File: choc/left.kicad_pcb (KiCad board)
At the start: 2 copper layers, 118 x 92 mm, 87 parts, among them J1 USB_B_Micro, SW1 SW_Push, SW10 SW_Push, SW11 SW_Push, SW12 SW_Push, SW13 SW_Push, SW14 SW_Push, SW15 SW_Push, SW16 SW_Push, SW17 SW_Push, SW18 SW_Push, SW19 SW_Push, SW2 SW_Push, SW20 SW_Push, SW21 SW_Push, SW22 SW_Push, SW23 SW_Push, SW3 SW_Push, SW4 SW_Push, SW47 SW_Push, SW49 SW_Push, SW5 SW_Push, SW6 SW_Push, SW7 SW_Push, SW8 SW_Push, SW9 SW_Push, U1 ProMicro

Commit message: progress
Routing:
- net GND: track 0.00 -> 753.6 mm, vias 0 -> 5
- net +5V: track 0.00 -> 578.4 mm, vias 0 -> 7
- net /lcol0: track 0.00 -> 183.0 mm, vias 0 -> 2
- net /lcol2: track 0.00 -> 176.5 mm, vias 0 -> 3
- net /lcol3: track 0.00 -> 174.6 mm, vias 0 -> 3
- net /lcol1: track 0.00 -> 156.9 mm, vias 0 -> 4
- net /lcol4: track 0.00 -> 111.5 mm, vias 0 -> 1
- net Net-(LED1-Pad4): track 0.00 -> 106.6 mm, vias 0 -> 2
- net /lrow4: track 0.00 -> 105.1 mm
- net /lrow0: track 0.00 -> 97.8 mm
- net Net-(LED23-Pad2): track 0.00 -> 96.3 mm
- net Net-(D2-Pad2): track 0.00 -> 96.1 mm
- net Net-(D3-Pad2): track 0.00 -> 87.8 mm, vias 0 -> 1
- net Net-(LED2-Pad4): track 0.00 -> 87.7 mm, vias 0 -> 2
- net /lrow1: track 0.00 -> 83.8 mm, vias 0 -> 2
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
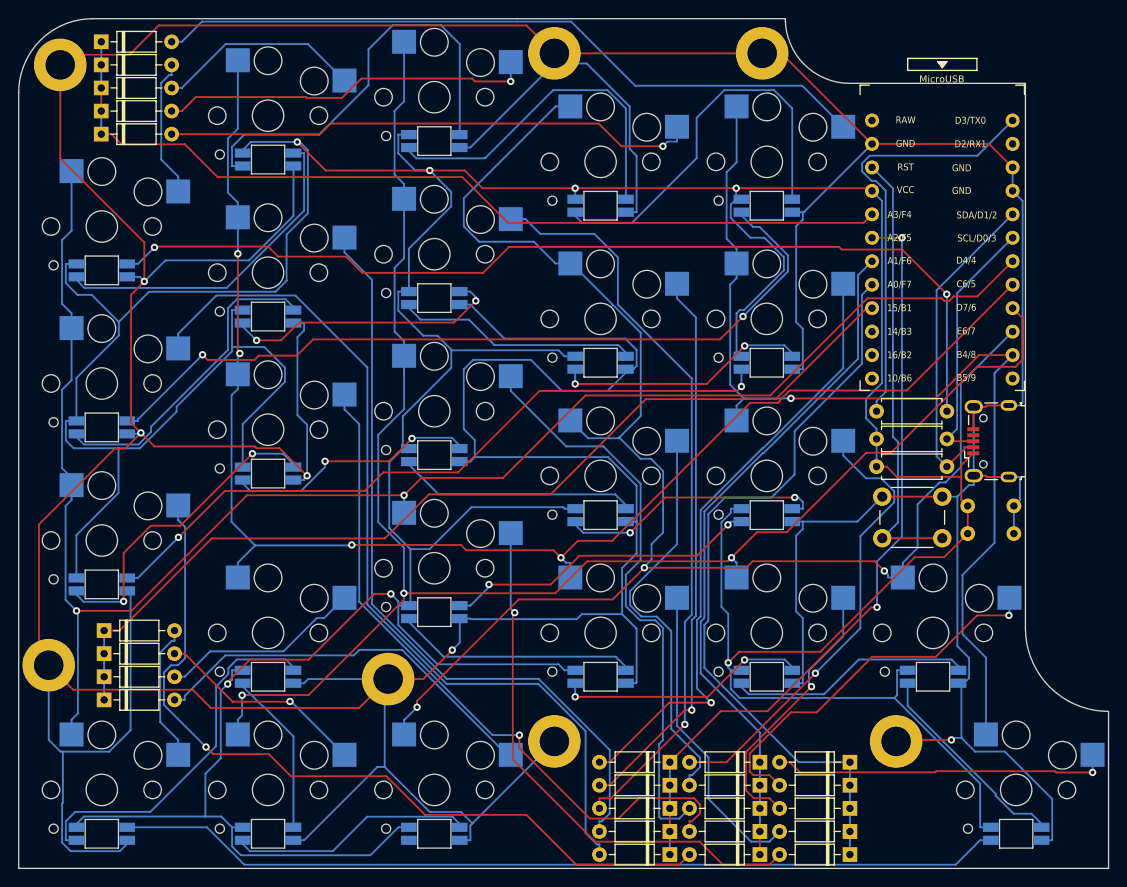
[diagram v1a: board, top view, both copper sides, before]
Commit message: add routed left board
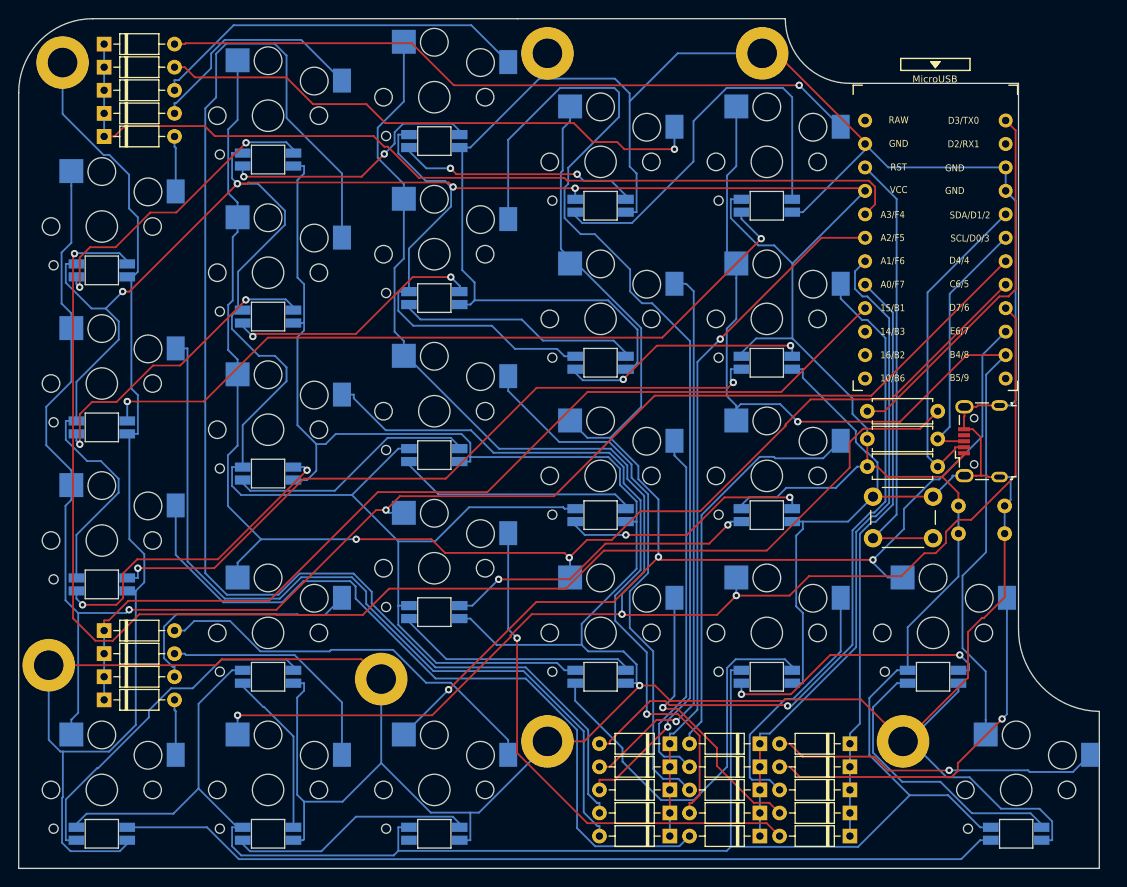
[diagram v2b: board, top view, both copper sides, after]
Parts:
- moved D1 7.76 mm to (25.2, 31.0)
- moved D47 7.50 mm to (25.2, 84.5)
- moved D5 7.50 mm to (25.2, 92.0)
- moved D16 7.26 mm to (25.2, 23.5)
- moved D6 2.77 mm to (25.2, 28.5)
- moved D11 2.27 mm to (25.2, 26.0)
- moved D12 2.00 mm to (86.5, 101.8)
- moved D13 2.00 mm to (96.2, 101.8)
- moved D14 2.00 mm to (106.0, 101.8)
- moved D17 2.00 mm to (86.5, 99.2)
- moved D18 2.00 mm to (96.2, 99.2)
- moved D19 2.00 mm to (106.0, 99.2)
- moved D2 2.00 mm to (86.5, 106.8)
- moved D21 2.00 mm to (86.5, 96.8)
- moved D22 2.00 mm to (96.2, 96.8)
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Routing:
- net Net-(D7-Pad2): track 82.6 -> 148.3 mm
- net GND: track 753.6 -> 700.8 mm, vias 5 -> 1
- net Net-(LED1-Pad4): track 106.6 -> 152.5 mm, vias 2 -> 1
- net Net-(D12-Pad2): track 81.2 -> 113.3 mm
- net /lcol2: track 176.5 -> 202.6 mm
- net /lrow3: track 81.9 -> 63.1 mm
- net /lcol3: track 174.6 -> 156.0 mm
- net Net-(LED11-Pad4): track 46.3 -> 28.4 mm, vias 0 -> 2
- net Net-(LED14-Pad4): track 27.3 -> 44.0 mm, vias 2 -> 0
- net +5V: track 578.4 -> 590.4 mm, vias 7 -> 4
- net Net-(LED11-Pad2): track 37.9 -> 26.3 mm, vias 0 -> 2
- net Net-(D1-Pad2): track 15.1 -> 6.00 mm
- net Net-(D5-Pad2): track 15.1 -> 6.00 mm
- net Net-(LED19-Pad2): track 22.7 -> 31.5 mm
- net Net-(D21-Pad2): track 67.4 -> 75.6 mm
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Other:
- board size 118 x 92 mm -> 117 x 92 mm

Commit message: remove leds from choc
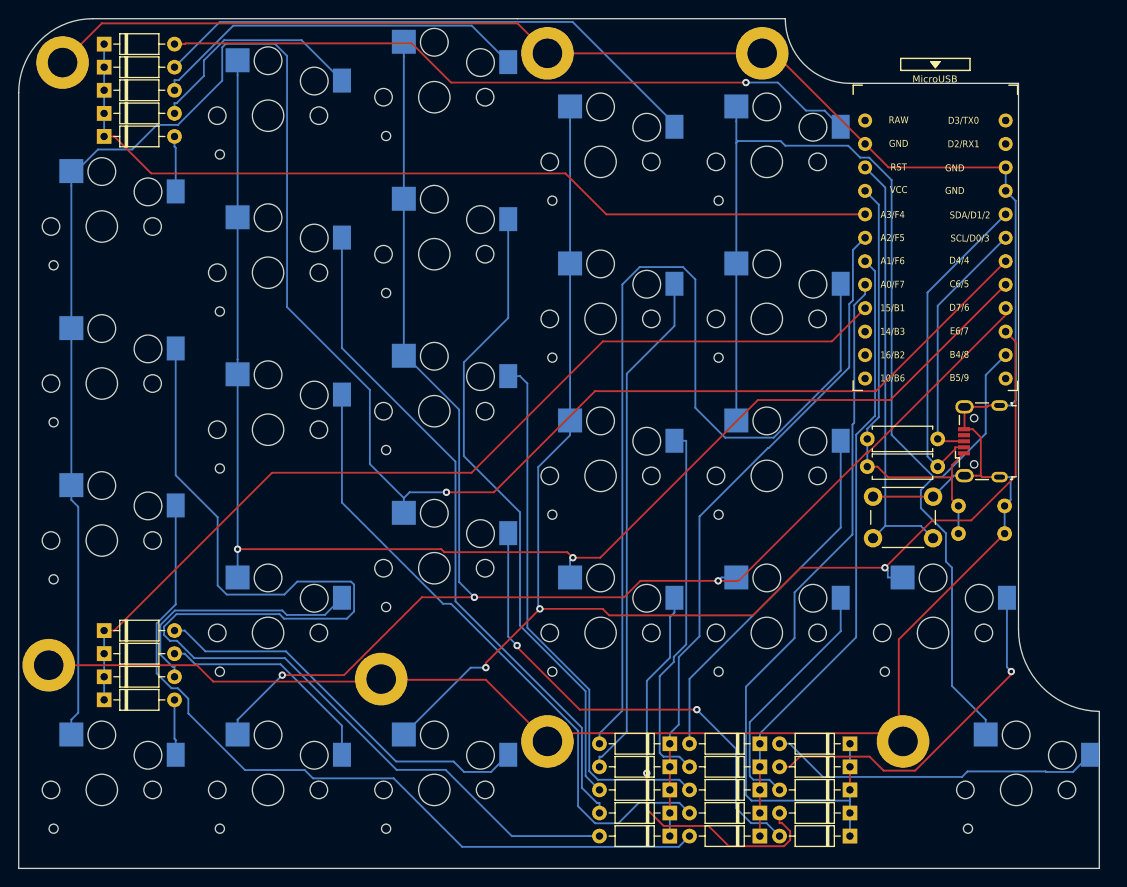
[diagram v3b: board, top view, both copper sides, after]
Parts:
- removed LED1, LED10, LED11, LED12, LED13, LED14, LED15, LED16, LED17, LED18, LED19, LED2, LED20, LED21, LED22, LED23, LED3, LED4, LED47, LED5, LED6, LED7, LED8, LED9: YS-SK6812MINI-E, kbd:YS-SK6812MINI-E
- removed R5: 1k, Resistor_THT:R_Axial_DIN0207_L6.3mm_D2.5mm_P7.62mm_Horizontal
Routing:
- net +5V: track 590.4 -> 50.2 mm, vias 4 -> 0
- net GND: track 700.8 -> 296.5 mm, vias 1 -> 0
- net Net-(LED1-Pad4): track 152.5 -> 0.00 mm, vias 1 -> 0
- net Net-(LED23-Pad2): track 95.8 -> 0.00 mm
- net Net-(LED2-Pad4): track 81.8 -> 0.00 mm, vias 2 -> 0
- net Net-(LED21-Pad2): track 77.7 -> 0.00 mm, vias 2 -> 0
- net Net-(D7-Pad2): track 148.3 -> 74.0 mm
- net Net-(LED16-Pad2): track 44.3 -> 0.00 mm
- net Net-(LED14-Pad4): track 44.0 -> 0.00 mm
- net Net-(D12-Pad2): track 113.3 -> 69.9 mm, vias 1 -> 0
- net /lcol0: track 183.5 -> 224.0 mm, vias 2 -> 1
- net /lLED: track 40.3 -> 0.00 mm
- net Net-(LED10-Pad4): track 37.7 -> 0.00 mm
- net Net-(D2-Pad2): track 89.7 -> 125.1 mm
- net Net-(LED3-Pad2): track 35.3 -> 0.00 mm, vias 2 -> 0
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
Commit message: add buzzer to pcb
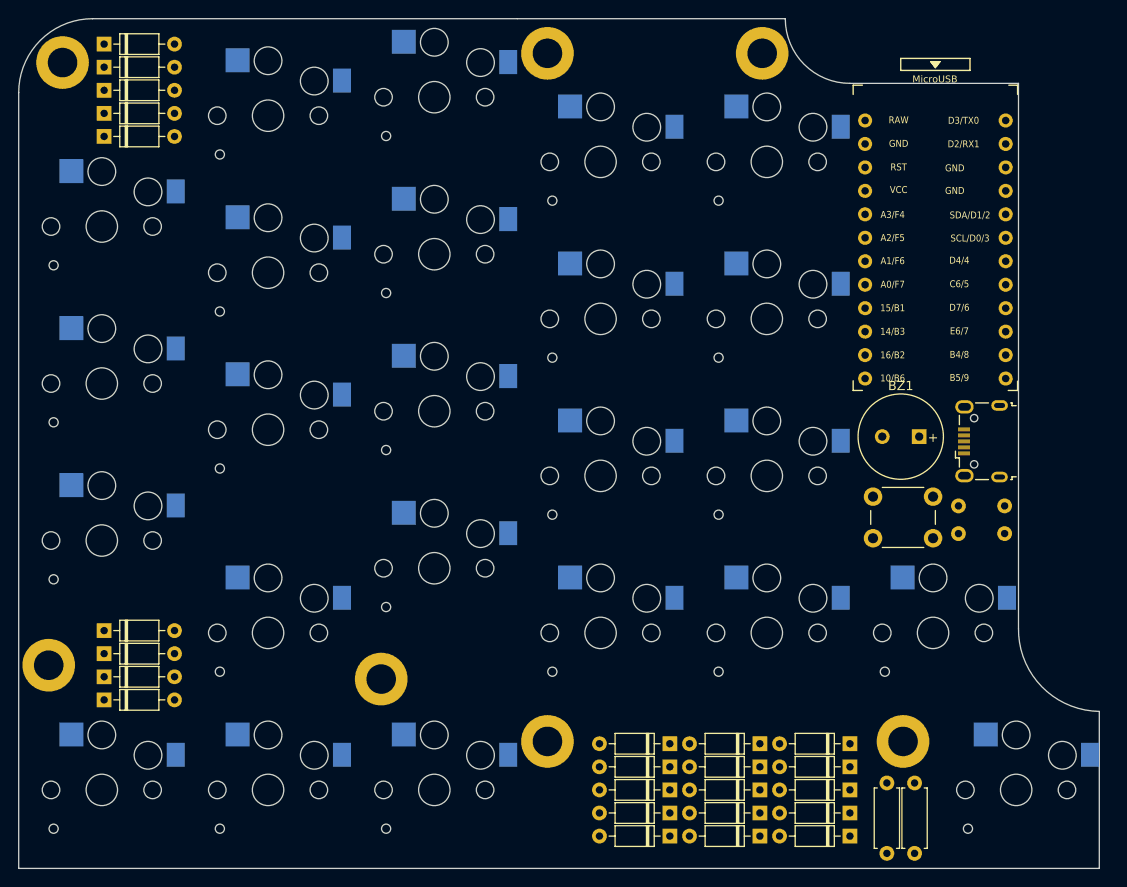
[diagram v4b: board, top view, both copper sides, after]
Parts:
- added BZ1: Buzzer, Buzzer_Beeper:MagneticBuzzer_PUI_AT-0927-TT-6-R, F.Cu at (113.5, 63.5)
- moved R1 37.7 mm to (110.0, 101.0), turned to -90 degrees
- moved R2 34.3 mm to (113.0, 101.0), turned to -90 degrees
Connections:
- U1 pad 12: unconnected-(U1-Pad12) -> /lbuzzer
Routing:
- net GND: track 296.5 -> 0.00 mm
- net /lcol0: track 224.0 -> 0.00 mm, vias 1 -> 0
- net /lcol2: track 169.2 -> 0.00 mm, vias 3 -> 0
- net /lcol1: track 154.1 -> 0.00 mm, vias 2 -> 0
- net /lcol3: track 153.5 -> 0.00 mm, vias 3 -> 0
- net /lcol4: track 135.0 -> 0.00 mm
- net Net-(D2-Pad2): track 125.1 -> 0.00 mm
- net /lrow4: track 104.4 -> 0.00 mm
- net Net-(D21-Pad2): track 103.4 -> 0.00 mm
- net /lrow0: track 95.9 -> 0.00 mm
- net Net-(D3-Pad2): track 85.9 -> 0.00 mm
- net /lrow3: track 82.1 -> 0.00 mm
- net Net-(D20-Pad2): track 75.9 -> 0.00 mm, vias 1 -> 0
- net Net-(D7-Pad2): track 74.0 -> 0.00 mm
- net /lrow1: track 73.6 -> 0.00 mm
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
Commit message: import left ses
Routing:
- net GND: track 0.00 -> 311.9 mm
- net /lcol0: track 0.00 -> 185.6 mm, vias 0 -> 1
- net /lcol1: track 0.00 -> 170.1 mm, vias 0 -> 2
- net /lcol2: track 0.00 -> 163.8 mm, vias 0 -> 2
- net /lcol3: track 0.00 -> 151.3 mm, vias 0 -> 3
- net /lcol4: track 0.00 -> 122.6 mm
- net Net-(D3-Pad2): track 0.00 -> 117.7 mm
- net /lrow4: track 0.00 -> 104.4 mm
- net /lrow0: track 0.00 -> 95.9 mm
- net Net-(D2-Pad2): track 0.00 -> 93.2 mm
- net +5V: track 0.00 -> 89.8 mm
- net Net-(D21-Pad2): track 0.00 -> 86.2 mm
- net Net-(D20-Pad2): track 0.00 -> 78.9 mm
- net Net-(D7-Pad2): track 0.00 -> 76.3 mm, vias 0 -> 1
- net /lSCL: track 0.00 -> 73.8 mm, vias 0 -> 1
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
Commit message: fix left
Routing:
- net Net-(D21-Pad2): track 86.2 -> 89.7 mm
- net /lrow1: track 73.5 -> 75.9 mm
- net Net-(D47-Pad2): track 50.8 -> 52.3 mm
- net Net-(D23-Pad2): track 46.1 -> 47.0 mm
- net Net-(D3-Pad2): track 117.7 -> 118.5 mm
- net Net-(D12-Pad2): track 66.8 -> 66.0 mm
- net Net-(D15-Pad2): track 27.1 -> 27.9 mm
- net Net-(D2-Pad2): track 93.2 -> 93.9 mm
